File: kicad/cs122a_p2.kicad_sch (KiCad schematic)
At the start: 19 parts, among them Q1 PN2222A, SW1 SW_Tap, SW2 SW_Inc, SW3 SW_Dec, U1 STM32F042K6Tx, U2 Digit 1, U3 Digit 2, U4 Digit 3, U5 SN7447A

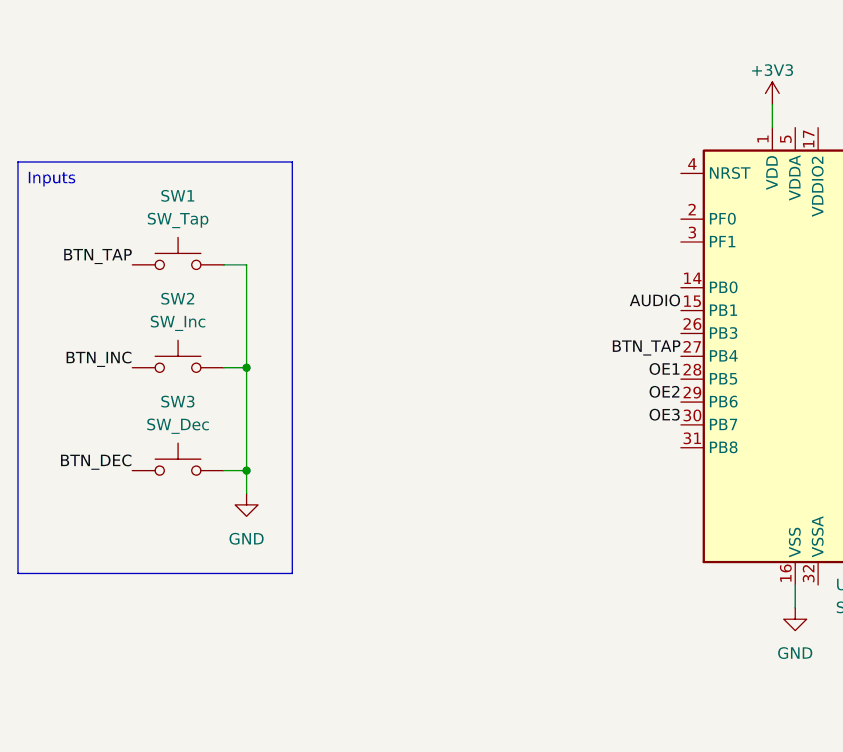
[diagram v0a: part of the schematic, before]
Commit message: Updated schematic with rhythm button
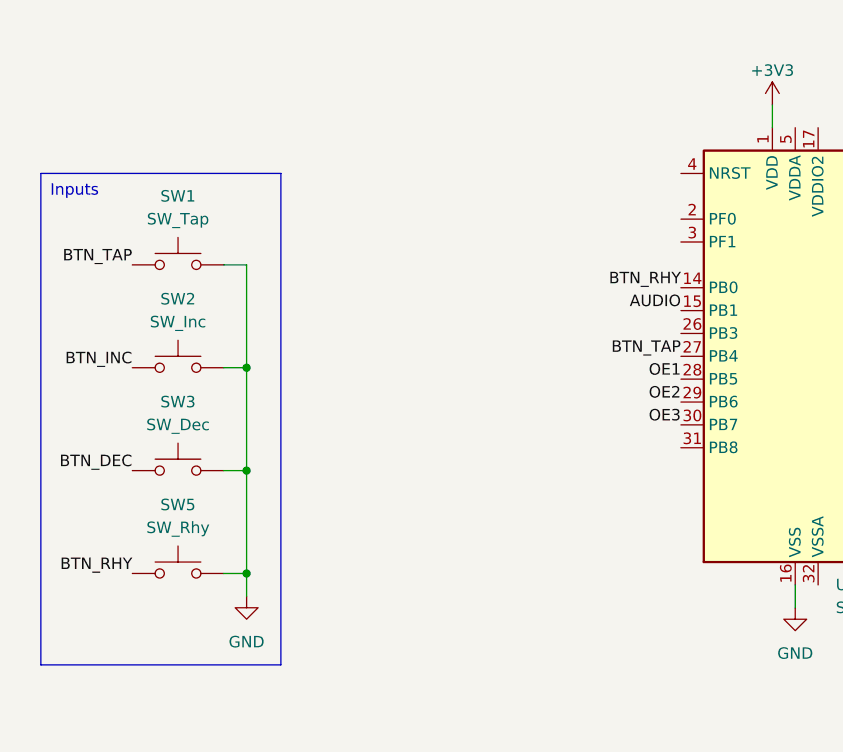
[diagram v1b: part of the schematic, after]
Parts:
- added SW5: SW_Rhy, symbol Switch:SW_Push
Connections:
- net GND: now also SW5.2
- net BTN_RHY: now reaches U1.14 (PB0)
- net BTN_RHY: now also SW5.1
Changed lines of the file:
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@@
 (kicad_sch (version 20230121) (generator eeschema)
   (paper "A4")
+  (junction (at 74.93 128.27) (diameter 0) (color 0 0 0 0)
+  )
   (junction (at 74.93 105.41) (diameter 0) (color 0 0 0 0)
   )
@@
     (stroke (width 0) (type default))
   )
-  (wire (pts (xy 74.93 119.38) (xy 74.93 116.84))
+  (wire (pts (xy 74.93 130.81) (xy 74.93 128.27))
     (stroke (width 0) (type default))
   )
@@
     (stroke (width 0) (type default))
   )
+  (wire (pts (xy 74.93 128.27) (xy 74.93 116.84))
+    (stroke (width 0) (type default))
+  )
   (wire (pts (xy 195.58 125.73) (xy 195.58 123.19))
     (stroke (width 0) (type default))
@@
   )
   (wire (pts (xy 209.55 120.65) (xy 209.55 110.49))
+    (stroke (width 0) (type default))
+  )
+  (wire (pts (xy 74.93 128.27) (xy 72.39 128.27))
     (stroke (width 0) (type default))
   )
@@
   )
   (text_box "Inputs"
-    (at 49.53 82.55 0) (size 30.48 45.72)
+    (at 52.07 83.82 0) (size 26.67 54.61)
     (stroke (width 0) (type default))
     (fill (type none))
@@
     (effects (font (size 1.27 1.27)) (justify right bottom))
   )
+  (label "BTN_RHY" (at 62.23 128.27 180) (fields_autoplaced)
+    (effects (font (size 1.27 1.27)) (justify right bottom))
+  )
   (label "SEG_F" (at 252.73 49.53 180) (fields_autoplaced)
     (effects (font (size 1.27 1.27)) (justify right bottom))
@@
   )
   (label "BTN_DEC" (at 62.23 116.84 180) (fields_autoplaced)
+    (effects (font (size 1.27 1.27)) (justify right bottom))
+  )
+  (label "BTN_RHY" (at 123.19 96.52 180) (fields_autoplaced)
     (effects (font (size 1.27 1.27)) (justify right bottom))
   )
@@
     )
   )
-  (symbol (lib_id "power:GND") (at 74.93 119.38 0) (unit 1)
-    (in_bom yes) (on_board yes) (dnp no) (fields_autoplaced)
-    (property "Reference" "#PWR06" (at 74.93 125.73 0)
-      (effects (font (size 1.27 1.27)) hide)
-    )
-    (property "Value" "GND" (at 74.93 124.46 0)
-      (effects (font (size 1.27 1.27)))
-    )
-    (property "Footprint" "" (at 74.93 119.38 0)
-      (effects (font (size 1.27 1.27)) hide)
-    )
-    (property "Datasheet" "" (at 74.93 119.38 0)
+  (symbol (lib_id "power:GND") (at 74.93 130.81 0) (unit 1)
+    (in_bom yes) (on_board yes) (dnp no) (fields_autoplaced)
+    (property "Reference" "#PWR06" (at 74.93 137.16 0)
+      (effects (font (size 1.27 1.27)) hide)
+    )
+    (property "Value" "GND" (at 74.93 135.89 0)
+      (effects (font (size 1.27 1.27)))
+    )
+    (property "Footprint" "" (at 74.93 130.81 0)
+      (effects (font (size 1.27 1.27)) hide)
+    )
+    (property "Datasheet" "" (at 74.93 130.81 0)
       (effects (font (size 1.27 1.27)) hide)
     )
@@
         )
       )
+    )
+  )
+  (symbol (lib_id "Switch:SW_Push") (at 67.31 128.27 0) (unit 1)
+    (in_bom yes) (on_board yes) (dnp no) (fields_autoplaced)
+    (property "Reference" "SW5" (at 67.31 120.65 0)
+      (effects (font (size 1.27 1.27)))
+    )
+    (property "Value" "SW_Rhy" (at 67.31 123.19 0)
+      (effects (font (size 1.27 1.27)))
+    )
+    (property "Footprint" "" (at 67.31 123.19 0)
+      (effects (font (size 1.27 1.27)) hide)
+    )
+    (property "Datasheet" "~" (at 67.31 123.19 0)
+      (effects (font (size 1.27 1.27)) hide)
+    )
+    (pin "1")
+    (pin "2")
+    (instances
+      (project "cs122a_p2"
+        (path "/f5250a06-5d3f-42a4-81bc-c043e883a187"
+          (reference "SW5") (unit 1)
+        )
+      )
